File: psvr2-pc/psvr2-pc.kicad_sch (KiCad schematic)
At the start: 91 parts, among them IC1 SN65MLVD200D, IC2 SN65MLVD200D, J1 USB_C_Receptacle, J2 USB3_B_Micro, J3 DP_47272, J4 Barrel_Jack_Switch, J5 Conn_01x02_Pin, Q1 Si2301CDS, Q2 PN2222A, Q3 Si2301CDS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

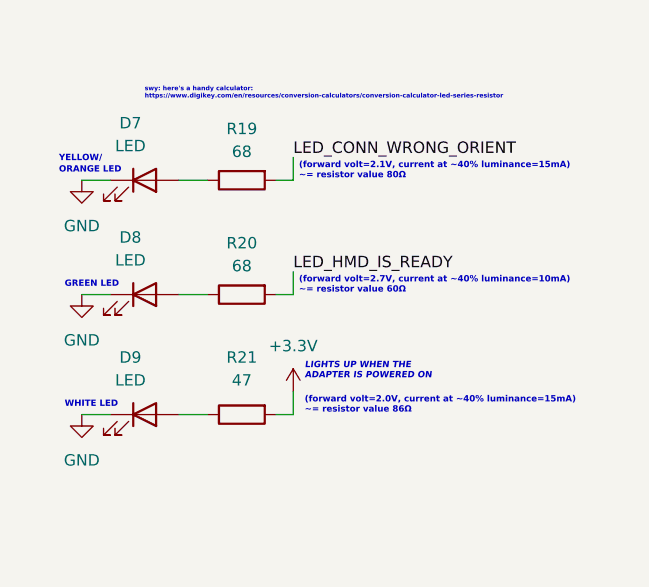
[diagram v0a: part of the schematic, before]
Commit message: Fix the white LED part number and use a much bigger resistor to make it dimmer. As this one is kind of strong. Hopefully things end up looking alright.
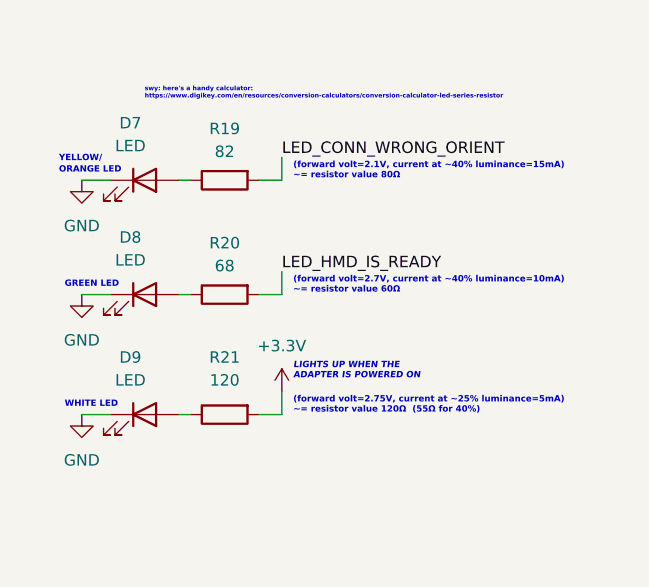
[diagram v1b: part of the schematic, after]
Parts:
- D9: LCSC Part # C84256 -> C34499; Mfr. Part # NCD0805R1 -> KT-0805W
- R19: value 68 -> 82
- R21: value 47 -> 120
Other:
- note added: "(forward volt=2.75V, current at ~25% luminance=5mA) ~= resistor value 120Ω (55Ω for 40%)"
- note removed: "(forward volt=2.0V, current at ~40% luminance=15mA) ~= resistor value 86Ω"
- moved on the sheet: R19, R20, R21
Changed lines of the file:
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@@
     (stroke (width 0) (type default))
   )
-  (wire (pts (xy 374.015 49.53) (xy 375.92 49.53))
+  (wire (pts (xy 372.11 49.53) (xy 374.65 49.53))
     (stroke (width 0) (type default))
   )
@@
     (stroke (width 0) (type default))
   )
-  (wire (pts (xy 363.22 36.195) (xy 366.395 36.195))
+  (wire (pts (xy 363.22 36.195) (xy 364.49 36.195))
     (stroke (width 0) (type default))
   )
@@
     (stroke (width 0) (type default))
   )
-  (wire (pts (xy 375.92 46.99) (xy 375.92 49.53))
+  (wire (pts (xy 374.65 46.99) (xy 374.65 49.53))
     (stroke (width 0) (type default))
   )
@@
     (stroke (width 0) (type default))
   )
-  (wire (pts (xy 363.22 49.53) (xy 366.395 49.53))
+  (wire (pts (xy 363.22 49.53) (xy 364.49 49.53))
     (stroke (width 0) (type default))
   )
@@
     (stroke (width 0) (type default))
   )
-  (wire (pts (xy 374.015 23.495) (xy 375.92 23.495))
+  (wire (pts (xy 372.11 23.495) (xy 374.65 23.495))
     (stroke (width 0) (type default))
   )
-  (wire (pts (xy 374.015 36.195) (xy 375.92 36.195))
+  (wire (pts (xy 372.11 36.195) (xy 374.65 36.195))
     (stroke (width 0) (type default))
   )
@@
     (stroke (width 0) (type default))
   )
-  (wire (pts (xy 375.92 33.655) (xy 375.92 36.195))
+  (wire (pts (xy 374.65 33.655) (xy 374.65 36.195))
     (stroke (width 0) (type default))
   )
@@
     (stroke (width 0) (type default))
   )
-  (wire (pts (xy 363.22 23.495) (xy 366.395 23.495))
+  (wire (pts (xy 363.22 23.495) (xy 364.49 23.495))
     (stroke (width 0) (type default))
   )
@@
     (stroke (width 0) (type default))
   )
-  (wire (pts (xy 375.92 20.955) (xy 375.92 23.495))
+  (wire (pts (xy 374.65 20.955) (xy 374.65 23.495))
     (stroke (width 0) (type default))
   )
@@
   )
   (text "(forward volt=2.1V, current at ~40% luminance=15mA)\n~= resistor value 80Ω "
-    (at 376.555 23.495 0)
+    (at 375.92 23.495 0)
     (effects (font (size 0.7 0.7) bold) (justify left bottom))
   )
@@
     (effects (font (size 0.7 0.7) bold) (justify left bottom))
   )
-  (text "(forward volt=2.0V, current at ~40% luminance=15mA)\n~= resistor value 86Ω "
-    (at 377.19 49.53 0)
+  (text "(forward volt=2.75V, current at ~25% luminance=5mA)\n~= resistor value 120Ω  (55Ω for 40%)"
+    (at 375.92 49.53 0)
     (effects (font (size 0.7 0.7) bold) (justify left bottom))
   )
   (text "(forward volt=2.7V, current at ~40% luminance=10mA)\n~= resistor value 60Ω"
-    (at 376.555 36.195 0)
+    (at 375.92 36.195 0)
     (effects (font (size 0.7 0.7) bold) (justify left bottom))
   )
@@
     (effects (font (face "Courier New") (size 1.27 1.27) (thickness 0.254) bold) (justify left bottom))
   )
-  (text "LIGHTS UP WHEN THE\nADAPTER IS POWERED ON" (at 377.19 45.72 0)
+  (text "LIGHTS UP WHEN THE\nADAPTER IS POWERED ON" (at 375.92 45.72 0)
     (effects (font (size 0.7 0.7) bold italic) (justify left bottom))
   )
@@
     (effects (font (size 1.27 1.27)) (justify left bottom))
   )
-  (label "LED_CONN_WRONG_ORIENT" (at 375.92 20.955 0) (fields_autoplaced)
+  (label "LED_CONN_WRONG_ORIENT" (at 374.65 20.955 0) (fields_autoplaced)
     (effects (font (size 1.27 1.27)) (justify left bottom))
   )
@@
     (effects (font (size 1.27 1.27)) (justify left bottom))
   )
-  (label "LED_HMD_IS_READY" (at 375.92 33.655 0) (fields_autoplaced)
+  (label "LED_HMD_IS_READY" (at 374.65 33.655 0) (fields_autoplaced)
     (effects (font (size 1.27 1.27)) (justify left bottom))
   )
@@
     )
   )
-  (symbol (lib_id "Device:R") (at 370.205 36.195 90) (mirror x) (unit 1)
+  (symbol (lib_id "Device:R") (at 368.3 36.195 90) (mirror x) (unit 1)
     (in_bom yes) (on_board yes) (dnp no) (fields_autoplaced)
-    (property "Reference" "R20" (at 370.205 30.48 90)
+    (property "Reference" "R20" (at 368.3 30.48 90)
       (effects (font (size 1.27 1.27)))
     )
-    (property "Value" "68" (at 370.205 33.02 90)
+    (property "Value" "68" (at 368.3 33.02 90)
       (effects (font (size 1.27 1.27)))
     )
-    (property "Footprint" "Resistor_SMD:R_0805_2012Metric" (at 370.205 34.417 90)
+    (property "Footprint" "Resistor_SMD:R_0805_2012Metric" (at 368.3 34.417 90)
       (effects (font (size 1.27 1.27)) hide)
     )
-    (property "Datasheet" "~" (at 370.205 36.195 0)
+    (property "Datasheet" "~" (at 368.3 36.195 0)
       (effects (font (size 1.27 1.27)) hide)
     )
@@
     )
   )
-  (symbol (lib_id "Device:R") (at 370.205 49.53 90) (mirror x) (unit 1)
+  (symbol (lib_id "Device:R") (at 368.3 49.53 90) (mirror x) (unit 1)
     (in_bom yes) (on_board yes) (dnp no) (fields_autoplaced)
-    (property "Reference" "R21" (at 370.205 43.18 90)
+    (property "Reference" "R21" (at 368.3 43.18 90)
       (effects (font (size 1.27 1.27)))
     )
-    (property "Value" "47" (at 370.205 45.72 90)
+    (property "Value" "120" (at 368.3 45.72 90)
       (effects (font (size 1.27 1.27)))
     )
-    (property "Footprint" "Resistor_SMD:R_0805_2012Metric" (at 370.205 47.752 90)
+    (property "Footprint" "Resistor_SMD:R_0805_2012Metric" (at 368.3 47.752 90)
       (effects (font (size 1.27 1.27)) hide)
     )
-    (property "Datasheet" "~" (at 370.205 49.53 0)
+    (property "Datasheet" "~" (at 368.3 49.53 0)
       (effects (font (size 1.27 1.27)) hide)
     )
@@
     )
   )
-  (symbol (lib_id "power:+3.3V") (at 375.92 46.99 0) (mirror y) (unit 1)
+  (symbol (lib_id "power:+3.3V") (at 374.65 46.99 0) (mirror y) (unit 1)
     (in_bom yes) (on_board yes) (dnp no) (fields_autoplaced)
-    (property "Reference" "#PWR028" (at 375.92 50.8 0)
+    (property "Reference" "#PWR028" (at 374.65 50.8 0)
       (effects (font (size 1.27 1.27)) hide)
     )
-    (property "Value" "+3.3V" (at 375.92 41.91 0)
+    (property "Value" "+3.3V" (at 374.65 41.91 0)
       (effects (font (size 1.27 1.27)))
     )
-    (property "Footprint" "" (at 375.92 46.99 0)
+    (property "Footprint" "" (at 374.65 46.99 0)
       (effects (font (size 1.27 1.27)) hide)
     )
-    (property "Datasheet" "" (at 375.92 46.99 0)
+    (property "Datasheet" "" (at 374.65 46.99 0)
       (effects (font (size 1.27 1.27)) hide)
     )
@@
     )
   )
-  (symbol (lib_id "Device:R") (at 370.205 23.495 90) (mirror x) (unit 1)
+  (symbol (lib_id "Device:R") (at 368.3 23.495 90) (mirror x) (unit 1)
     (in_bom yes) (on_board yes) (dnp no) (fields_autoplaced)
-    (property "Reference" "R19" (at 370.205 17.78 90)
+    (property "Reference" "R19" (at 368.3 17.78 90)
       (effects (font (size 1.27 1.27)))
     )
-    (property "Value" "68" (at 370.205 20.32 90)
+    (property "Value" "82" (at 368.3 20.32 90)
       (effects (font (size 1.27 1.27)))
     )
-    (property "Footprint" "Resistor_SMD:R_0805_2012Metric" (at 370.205 21.717 90)
+    (property "Footprint" "Resistor_SMD:R_0805_2012Metric" (at 368.3 21.717 90)
       (effects (font (size 1.27 1.27)) hide)
     )
-    (property "Datasheet" "~" (at 370.205 23.495 0)
+    (property "Datasheet" "~" (at 368.3 23.495 0)
       (effects (font (size 1.27 1.27)) hide)
     )
@@
       (effects (font (size 1.27 1.27)) hide)
     )
-    (property "Datasheet" "https://datasheet.lcsc.com/lcsc/2304140030_Foshan-NationStar-Optoelectronics-NCD0805R1_C84256.pdf" (at 359.41 49.53 0)
+    (property "Datasheet" "https://datasheet.lcsc.com/lcsc/2305091500_Hubei-KENTO-Elec-KT-0805W_C34499.pdf" (at 359.41 49.53 0)
       (effects (font (size 1.27 1.27)) hide)
     )
-    (property "Mfr. Part #" "NCD0805R1" (at 359.41 49.53 0)
+    (property "Mfr. Part #" "KT-0805W" (at 359.41 49.53 0)
       (effects (font (size 1.27 1.27)) hide)
     )
-    (property "LCSC Part #" "C84256" (at 359.41 49.53 0)
+    (property "LCSC Part #" "C34499" (at 359.41 49.53 0)
       (effects (font (size 1.27 1.27)) hide)
     )

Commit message: Exclude the solder jumpers from the bill of materials, not sure why they were there. Add the part ID and datasheet to the DisplayPort connector.
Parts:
- J3: Field5 (none) -> 472720001; LCSC Part # (none) -> C587824
- JP1, JP2, JP3, JP4, JP5, JP6: now left out of the parts list
- SW1: LCSC Part # (none) -> C318884; LSC Part # C318884 -> (none)
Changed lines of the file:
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@@
   (text "(forward volt=2.1V, current at ~40% luminance=15mA)\n~= resistor value 80Ω "
     (at 375.92 23.495 0)
-    (effects (font (size 0.7 0.7) bold) (justify left bottom))
+    (effects (font (size 0.7 0.7) (thickness 0.14) bold) (justify left bottom))
   )
   (text "DP\nSINK\nHOT-\nPLUG\nDETEC\nTION\nPULSE" (at 165.735 133.985 0)
@@
   (text "swy: here's a handy calculator:\nhttps://www.digikey.com/en/resources/conversion-calculators/conversion-calculator-led-series-resistor"
     (at 359.41 14.605 0)
-    (effects (font (size 0.5 0.5) bold) (justify left bottom))
+    (effects (font (size 0.5 0.5) (thickness 0.1) bold) (justify left bottom))
   )
   (text "DISPLAYPORT AUX\nPICO<->PSVR2" (at 155.575 133.985 0)
@@
   )
   (symbol (lib_id "Jumper:SolderJumper_2_Bridged") (at 315.595 161.29 180) (unit 1)
-    (in_bom yes) (on_board yes) (dnp no)
+    (in_bom no) (on_board yes) (dnp no)
     (property "Reference" "JP6" (at 315.595 158.75 0)
       (effects (font (size 1.27 1.27)) hide)
@@
       (effects (font (size 1.27 1.27)) hide)
     )
-    (property "LSC Part #" "C318884" (at 144.018 239.776 0)
+    (property "LCSC Part #" "C318884" (at 144.018 239.776 0)
       (effects (font (size 1.27 1.27)) hide)
     )
@@
   )
   (symbol (lib_id "Jumper:SolderJumper_2_Open") (at 247.015 118.11 180) (unit 1)
-    (in_bom yes) (on_board yes) (dnp no)
+    (in_bom no) (on_board yes) (dnp no)
     (property "Reference" "JP2" (at 247.015 115.57 0)
       (effects (font (size 1.27 1.27)) hide)
@@
   )
   (symbol (lib_id "Jumper:SolderJumper_2_Open") (at 247.015 113.03 180) (unit 1)
-    (in_bom yes) (on_board yes) (dnp no)
+    (in_bom no) (on_board yes) (dnp no)
     (property "Reference" "JP1" (at 247.015 110.49 0)
       (effects (font (size 1.27 1.27)) hide)
@@
   )
   (symbol (lib_id "Jumper:SolderJumper_2_Bridged") (at 353.06 213.36 180) (unit 1)
-    (in_bom yes) (on_board yes) (dnp no)
+    (in_bom no) (on_board yes) (dnp no)
     (property "Reference" "JP4" (at 353.06 210.82 0)
       (effects (font (size 1.27 1.27)) hide)
@@
   )
   (symbol (lib_id "Jumper:SolderJumper_2_Bridged") (at 353.06 198.12 180) (unit 1)
-    (in_bom yes) (on_board yes) (dnp no)
+    (in_bom no) (on_board yes) (dnp no)
     (property "Reference" "JP3" (at 353.06 200.66 0)
       (effects (font (size 1.27 1.27)) hide)
@@
   )
   (symbol (lib_id "Jumper:SolderJumper_2_Bridged") (at 315.595 146.05 180) (unit 1)
-    (in_bom yes) (on_board yes) (dnp no)
+    (in_bom no) (on_board yes) (dnp no)
     (property "Reference" "JP5" (at 315.595 148.59 0)
       (effects (font (size 1.27 1.27)) hide)
@@
       (effects (font (size 1.27 1.27)) hide)
     )
+    (property "Field4" "" (at 27.94 95.25 0)
+      (effects (font (size 1.27 1.27)) hide)
+    )
+    (property "Field5" "" (at 27.94 95.25 0)
+      (effects (font (size 1.27 1.27)) hide)
+    )
     (pin "11")
     (pin "2")
@@
       (effects (font (size 1.27 1.27)) hide)
     )
-    (property "Datasheet" "" (at 34.29 12.7 0)
+    (property "Datasheet" "https://datasheet.lcsc.com/lcsc/2008191735_MOLEX-472720001_C587824.pdf" (at 34.29 12.7 0)
+      (effects (font (size 1.27 1.27)) hide)
+    )
+    (property "LCSC Part #" "C587824" (at 34.29 12.7 0)
+      (effects (font (size 1.27 1.27)) hide)
+    )
+    (property "Field5" "472720001" (at 34.29 12.7 0)
       (effects (font (size 1.27 1.27)) hide)
     )

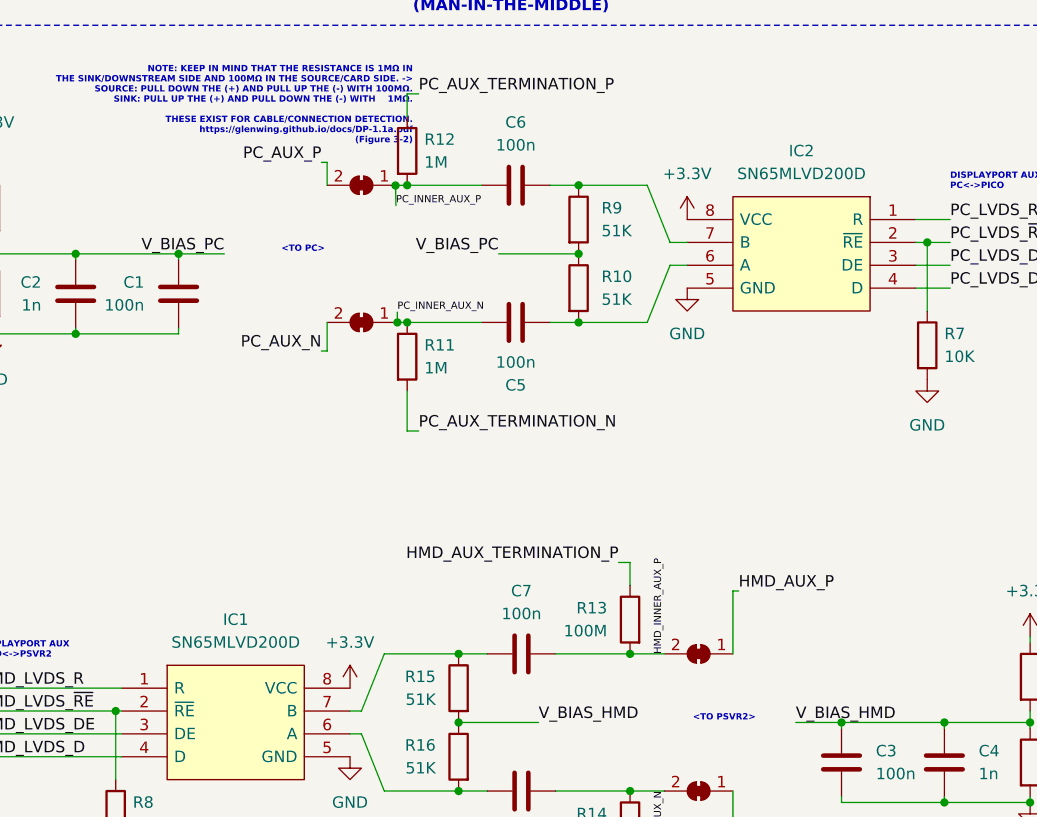
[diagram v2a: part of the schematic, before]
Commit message: Update the LVDS-M transceiver chip to the correct A model, as @mrandTX said: SN65MLVD200ADR:
--
@mrandTX
For anyone following along, and Swyter in particular, the following are all identical part numbers for 200A.  R specifies that it comes in a tape and reel packaging. G4 is extra green, although in this case, saying G4 doesn't matter - you seem to get G4 regardless if you specify it.
SN65MLVD200AD
SN65MLVD200ADG4
SN65MLVD200ADR
SN65MLVD200ADRG4
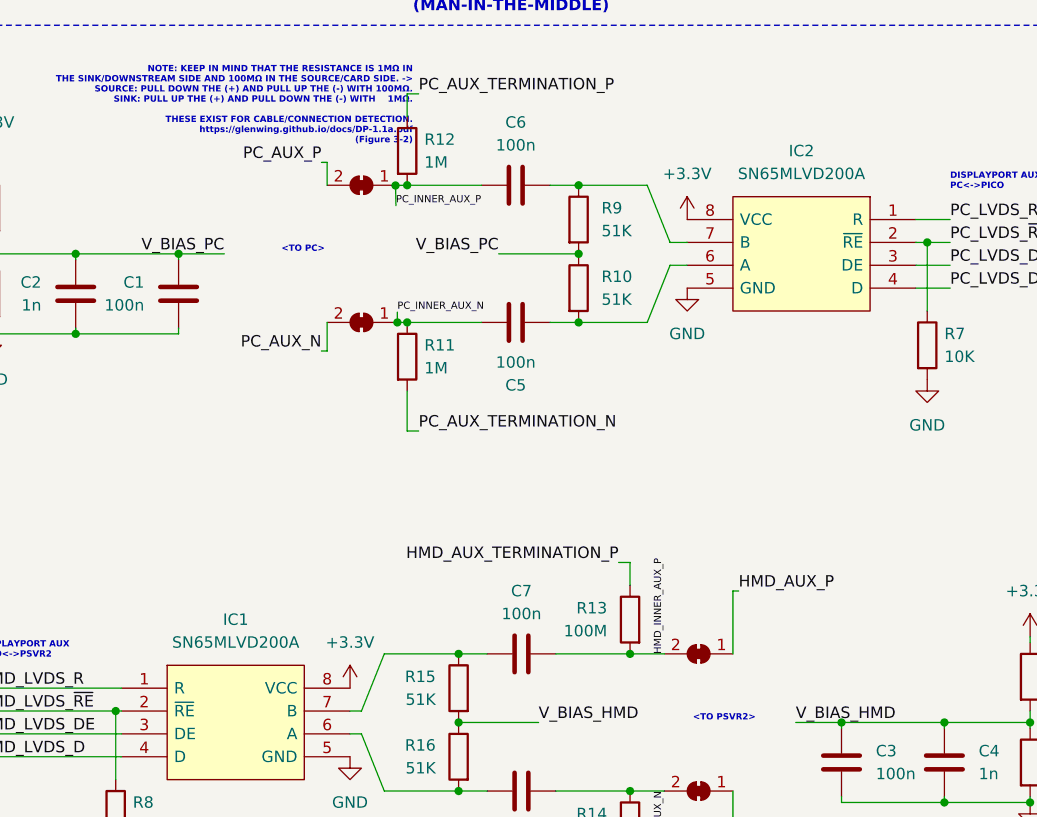
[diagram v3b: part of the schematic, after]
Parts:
- IC1, IC2: value SN65MLVD200D -> SN65MLVD200A; Arrow Part Number SN65MLVD200D -> SN65MLVD200A; LCSC Part # (none) -> C695776; Manufacturer_Part_Number SN65MLVD200D -> SN65MLVD200A; Mfr. Part # (none) -> SN65MLVD200ADR; Mouser Part Number 595-SN65MLVD200D -> 595-SN65MLVD200A
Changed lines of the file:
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@@
       (effects (font (size 1.27 1.27)))
     )
-    (property "Value" "SN65MLVD200D" (at 364.49 144.78 0)
+    (property "Value" "SN65MLVD200A" (at 364.49 144.78 0)
       (effects (font (size 1.27 1.27)))
     )
@@
       (effects (font (size 1.27 1.27)) (justify left) hide)
     )
-    (property "Manufacturer_Part_Number" "SN65MLVD200D" (at 355.6 160.02 0)
-      (effects (font (size 1.27 1.27)) (justify left) hide)
-    )
-    (property "Mouser Part Number" "595-SN65MLVD200D" (at 355.6 162.56 0)
+    (property "Manufacturer_Part_Number" "SN65MLVD200A" (at 355.6 160.02 0)
+      (effects (font (size 1.27 1.27)) (justify left) hide)
+    )
+    (property "Mouser Part Number" "595-SN65MLVD200A" (at 355.6 162.56 0)
       (effects (font (size 1.27 1.27)) (justify left) hide)
     )
@@
       (effects (font (size 1.27 1.27)) (justify left) hide)
     )
-    (property "Arrow Part Number" "SN65MLVD200D" (at 355.6 167.64 0)
+    (property "Arrow Part Number" "SN65MLVD200A" (at 355.6 167.64 0)
       (effects (font (size 1.27 1.27)) (justify left) hide)
     )
     (property "Arrow Price/Stock" "https://www.arrow.com/en/products/sn65mlvd200d/texas-instruments" (at 355.6 170.18 0)
       (effects (font (size 1.27 1.27)) (justify left) hide)
+    )
+    (property "LCSC Part #" "C695776" (at 377.19 149.86 0)
+      (effects (font (size 1.27 1.27)) hide)
+    )
+    (property "Mfr. Part #" "SN65MLVD200ADR" (at 377.19 149.86 0)
+      (effects (font (size 1.27 1.27)) hide)
     )
     (pin "8")
@@
       (effects (font (size 1.27 1.27)))
     )
-    (property "Value" "SN65MLVD200D" (at 301.625 196.85 0)
+    (property "Value" "SN65MLVD200A" (at 301.625 196.85 0)
       (effects (font (size 1.27 1.27)))
     )
@@
       (effects (font (size 1.27 1.27)) (justify left) hide)
     )
-    (property "Manufacturer_Part_Number" "SN65MLVD200D" (at 310.515 212.09 0)
-      (effects (font (size 1.27 1.27)) (justify left) hide)
-    )
-    (property "Mouser Part Number" "595-SN65MLVD200D" (at 310.515 214.63 0)
+    (property "Manufacturer_Part_Number" "SN65MLVD200A" (at 310.515 212.09 0)
+      (effects (font (size 1.27 1.27)) (justify left) hide)
+    )
+    (property "Mouser Part Number" "595-SN65MLVD200A" (at 310.515 214.63 0)
       (effects (font (size 1.27 1.27)) (justify left) hide)
     )
@@
       (effects (font (size 1.27 1.27)) (justify left) hide)
     )
-    (property "Arrow Part Number" "SN65MLVD200D" (at 310.515 219.71 0)
+    (property "Arrow Part Number" "SN65MLVD200A" (at 310.515 219.71 0)
       (effects (font (size 1.27 1.27)) (justify left) hide)
     )
@@
       (effects (font (size 1.27 1.27)) (justify left) hide)
     )
+    (property "LCSC Part #" "C695776" (at 288.925 201.93 0)
+      (effects (font (size 1.27 1.27)) hide)
+    )
+    (property "Mfr. Part #" "SN65MLVD200ADR" (at 288.925 201.93 0)
+      (effects (font (size 1.27 1.27)) hide)
+    )
     (pin "8")
